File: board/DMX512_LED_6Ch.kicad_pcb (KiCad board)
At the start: 2 copper layers, 75 x 55 mm, 68 parts, among them J1 XLR3, J2 XLR3, J3 Conn_01x02, J4 Conn_01x04, J5 Conn_01x04, J6 Conn_ARM_JTAG_SWD_10, J7 Conn_01x04, J8 USB_C_Receptacle_USB2.0, Q1 BSC028N06LS3, Q2 BSC028N06LS3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

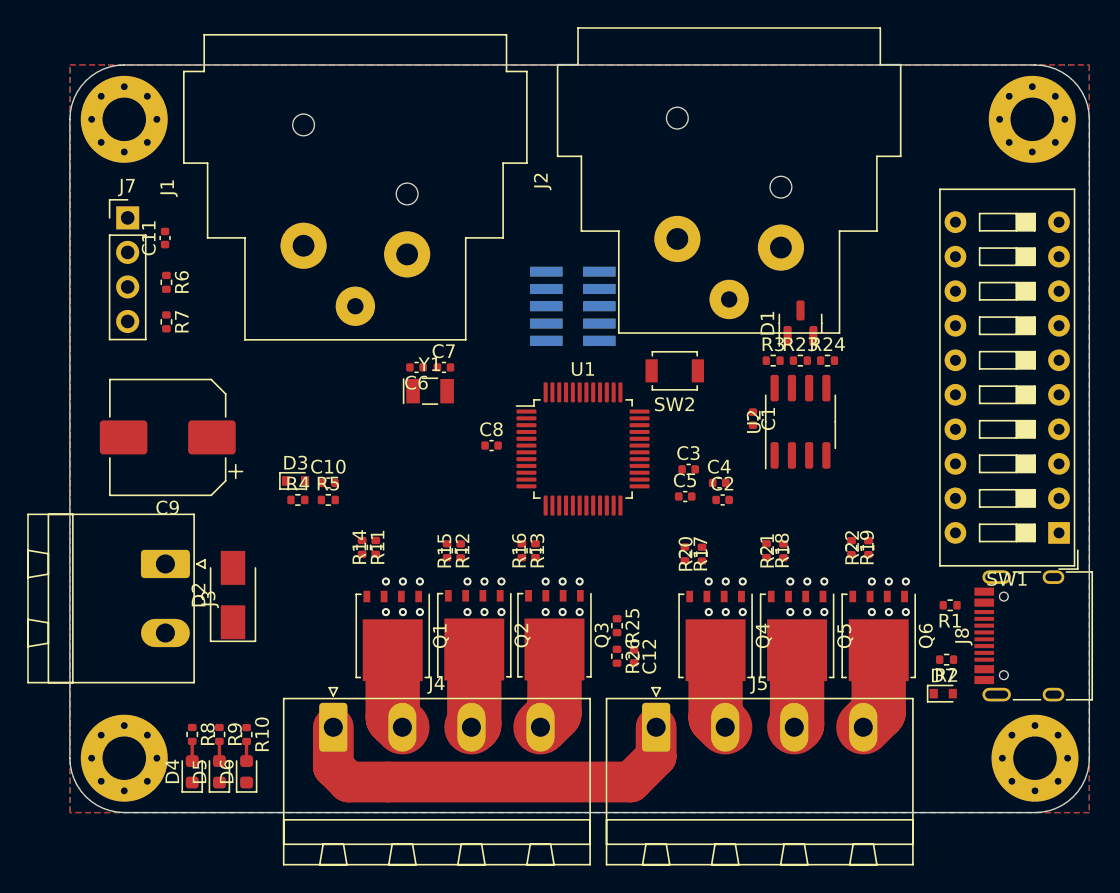
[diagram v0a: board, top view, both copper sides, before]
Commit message: doing some cost reduction
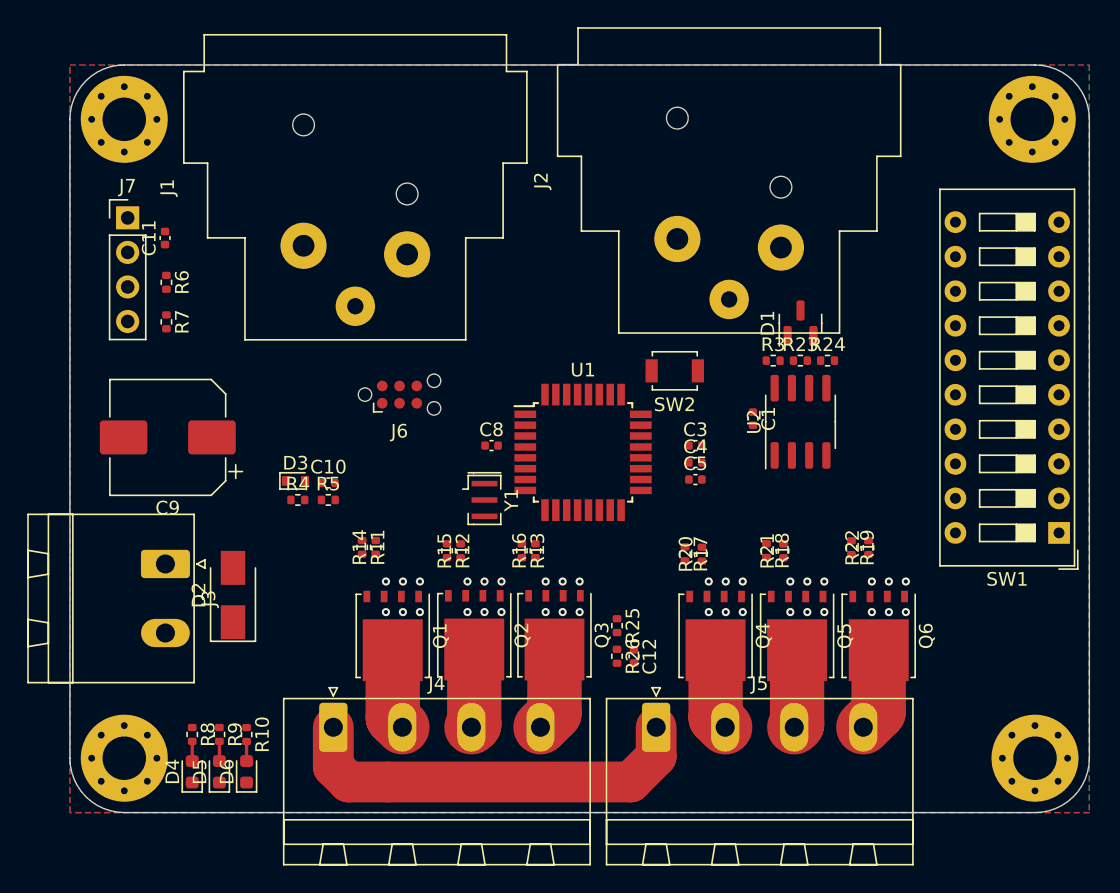
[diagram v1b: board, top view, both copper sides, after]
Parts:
- removed C2: 1uF, Capacitor_SMD:C_0402_1005Metric
- removed C6, C7: 22pF, Capacitor_SMD:C_0402_1005Metric
- removed D7: RB751V-40WS RRG, Diode_SMD:D_SOD-523
- removed J8: USB_C_Receptacle_USB2.0, Connector_USB:USB_C_Receptacle_HRO_TYPE-C-31-M-12
- removed R1, R2: 5k1, Resistor_SMD:R_0402_1005Metric
- J6: value Conn_ARM_JTAG_SWD_10 -> AVR-ISP-6; footprint Connector_PinHeader_1.27mm:PinHeader_2x05_P1.27mm_Vertical_SMD -> Connector:Tag-Connect_TC2030-IDC-NL_2x03_P1.27mm_Vertical; moved to F.Cu
- U1: value ATSAMD21G18A-A -> ATmega8A-A; footprint Package_QFP:TQFP-48_7x7mm_P0.5mm -> Package_QFP:TQFP-32_7x7mm_P0.8mm
- Y1: value 32.768kHz -> 16MHz; footprint Crystal:Crystal_SMD_EuroQuartz_EQ161-2Pin_3.2x1.5mm -> Crystal:Resonator_SMD_Murata_CSTxExxV-3Pin_3.0x1.1mm
- moved J6 14.3 mm to (124.2, 104.2)
- moved Y1 8.94 mm to (130.5, 112.0), turned to -90 degrees
- moved C4 2.30 mm to (146.0, 109.2)
- moved C3 1.82 mm to (146.0, 108.0)
- moved C5 1.46 mm to (146.0, 110.5)
- moved U1 0.25 mm to (137.8, 108.5)
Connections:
- C3 pad 1: +3V3 -> +5V
- C4 pad 1: +3V3 -> +5V
- C5 pad 1: +3V3 -> +5V
- C8 pad 1: +3V3 -> +5V
- J6 pad 1: unconnected-(J6-Pad1) -> /MISO
- J6 pad 2: /SWD_DIO -> +5V
- J6 pad 3: GND -> /SCK
- J6 pad 4: /SWD_CLK -> /MOSI
- J6 pad 5: GND -> /~{RESET}
- J6 pad 6: unconnected-(J6-Pad6) -> GND
- R10 pad 1: unconnected-(R10-Pad1) -> /LED3
- R6 pad 1: +3V3 -> +5V
- R7 pad 1: +3V3 -> +5V
- R8 pad 1: unconnected-(R8-Pad1) -> /LED1
- R9 pad 1: unconnected-(R9-Pad1) -> /LED2
- U1 pad 1: Net-(C7-Pad2) -> /CH1_RED_EN
- U1 pad 10: unconnected-(U1-Pad10) -> /CH1_BLU_EN
- U1 pad 15: unconnected-(U1-Pad15) -> /MOSI
- U1 pad 16: unconnected-(U1-Pad16) -> /MISO
- U1 pad 17: +3V3 -> /SCK
- U1 pad 18: GND -> +5V
- U1 pad 19: unconnected-(U1-Pad19) -> /TMP_MON
- U1 pad 2: Net-(C6-Pad2) -> unconnected-(U1-Pad2)
- U1 pad 21: unconnected-(U1-Pad21) -> GND
- U1 pad 22: unconnected-(U1-Pad22) -> /VCC_MON
- U1 pad 27: unconnected-(U1-Pad27) -> /I2C_SDA
- U1 pad 28: unconnected-(U1-Pad28) -> /I2C_SCL
- U1 pad 29: unconnected-(U1-Pad29) -> /~{RESET}
- U1 pad 3: unconnected-(U1-Pad3) -> GND
- U1 pad 30: unconnected-(U1-Pad30) -> /DMX_IN
- U1 pad 31: /I2C_SDA -> /DMX_OUT
- U1 pad 32: /I2C_SCL -> /DMX_DIR
- U1 pad 4: unconnected-(U1-Pad4) -> +5V
- U1 pad 6: +3V3 -> +5V
- U1 pad 7: unconnected-(U1-Pad7) -> Net-(U1-Pad7)
- U1 pad 8: unconnected-(U1-Pad8) -> Net-(U1-Pad8)
- U1 pad 9: unconnected-(U1-Pad9) -> /CH1_GRN_EN
- Y1 pad 1: Net-(C6-Pad2) -> Net-(U1-Pad7)
- Y1 pad 2: Net-(C7-Pad2) -> GND
